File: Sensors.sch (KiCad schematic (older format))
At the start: 69 parts, among them CON1 CONSOLE, IC1 ATMEGA328P, P1 CONN_01X08, P10 GPIO, P11 I2C, P12 96B-GPIO, P13 96B-I2C0, P14 GPIO, P15 GPIO, P16 GPIO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

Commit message: Switch transistor schematic symbol to BC817
The part is still an S8050, but we want to use the SOT-23 footprint
instead of TO-92. The default Kicad libraries don't have a SOT-23
version of the S8050, but it does have one for the BC817 which uses the
same pinout. Switch the schematic symbol so that KiCad stops complaining
about the footprint being different and needing to be "rescued"

Signed-off-by: Grant Likely <grant.likely@linaro.org>
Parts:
- Q1: symbol S8050 -> BC817-40
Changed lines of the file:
@@
 NoConn ~ 5550 6800
 $Comp
-L S8050 Q1
+L BC817-40 Q1
 U 1 1 55CE16C0
 P 5150 1600

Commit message: Get rid of "Sensors2" library
All of the footprints are stored in the "Sensors" library. The extra
"Sendors2" library is no longer needed. Replace all references to it
with "Sensors".

Signed-off-by: Grant Likely <grant.likely@linaro.org>
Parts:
- Q1, U5: footprint Sensors2:SOT-23_Seeed -> Sensors:SOT-23_Seeed
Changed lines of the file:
@@
 F 0 "U5" H 8150 2450 60  0000 C CNN
 F 1 "XC6206" H 8350 2450 60  0000 L CNN
-F 2 "Sensors2:SOT-23_Seeed" H 8150 2150 60  0001 C CNN
+F 2 "Sensors:SOT-23_Seeed" H 8150 2150 60  0001 C CNN
 F 3 "" H 8150 2150 60  0000 C CNN
 F 4 "310030016" H 2450 850 60  0001 C CNN "Seeed SKU"
@@
 F 0 "Q1" H 4900 1850 50  0000 L CNN
 F 1 "S8050" H 4900 1750 50  0000 L CNN
-F 2 "Sensors2:SOT-23_Seeed" H 5350 1525 50  0001 L CIN
+F 2 "Sensors:SOT-23_Seeed" H 5350 1525 50  0001 L CIN
 F 3 "" H 5150 1600 50  0000 L CNN
 	1    5150 1600

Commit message: Change resistor footprint for Seeed manufacturing
The default resistor footprint doesn't work for Seeed. Replace with the
footprint used on the UART board.

Signed-off-by: Grant Likely <grant.likely@linaro.org>
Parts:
- R1, R10, R11, R12, R13, R14, R15, R16, R2, R3, R4, R5, R6, R7, R8, R9: footprint Resistors_SMD:R_0603 -> Sensors:R_0603_Seeed
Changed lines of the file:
@@
 F 0 "R4" V 5330 750 50  0000 C CNN
 F 1 "10K" V 5250 750 50  0000 C CNN
-F 2 "Resistors_SMD:R_0603" V 5180 750 30  0001 C CNN
+F 2 "Sensors:R_0603_Seeed" V 5180 750 30  0001 C CNN
 F 3 "" H 5250 750 30  0000 C CNN
 F 4 "301010299" H 5250 750 60  0001 C CNN "Seeed SKU"
@@
 F 0 "R6" V 6330 750 50  0000 C CNN
 F 1 "620R" V 6250 750 50  0000 C CNN
-F 2 "Resistors_SMD:R_0603" V 6180 750 30  0001 C CNN
+F 2 "Sensors:R_0603_Seeed" V 6180 750 30  0001 C CNN
 F 3 "" H 6250 750 30  0000 C CNN
 F 4 "301010210" H 6250 750 60  0001 C CNN "Seeed SKU"
@@
 F 0 "R5" V 5580 750 50  0000 C CNN
 F 1 "620R" V 5500 750 50  0000 C CNN
-F 2 "Resistors_SMD:R_0603" V 5430 750 30  0001 C CNN
+F 2 "Sensors:R_0603_Seeed" V 5430 750 30  0001 C CNN
 F 3 "" H 5500 750 30  0000 C CNN
 F 4 "301010210" H 5500 750 60  0001 C CNN "Seeed SKU"
@@
 F 0 "R8" V 8080 6000 50  0000 C CNN
 F 1 "620R" V 8000 6000 50  0000 C CNN
-F 2 "Resistors_SMD:R_0603" V 7930 6000 30  0001 C CNN
+F 2 "Sensors:R_0603_Seeed" V 7930 6000 30  0001 C CNN
 F 3 "" H 8000 6000 30  0000 C CNN
 F 4 "301010210" H 2450 850 60  0001 C CNN "Seeed SKU"
@@
 F 0 "R9" V 8230 6000 50  0000 C CNN
 F 1 "620R" V 8150 6000 50  0000 C CNN
-F 2 "Resistors_SMD:R_0603" V 8080 6000 30  0001 C CNN
+F 2 "Sensors:R_0603_Seeed" V 8080 6000 30  0001 C CNN
 F 3 "" H 8150 6000 30  0000 C CNN
 F 4 "301010210" H 2450 850 60  0001 C CNN "Seeed SKU"
@@
 F 0 "R10" V 8380 6000 50  0000 C CNN
 F 1 "620R" V 8300 6000 50  0000 C CNN
-F 2 "Resistors_SMD:R_0603" V 8230 6000 30  0001 C CNN
+F 2 "Sensors:R_0603_Seeed" V 8230 6000 30  0001 C CNN
 F 3 "" H 8300 6000 30  0000 C CNN
 F 4 "301010210" H 2450 850 60  0001 C CNN "Seeed SKU"
@@
 F 0 "R11" V 8530 6000 50  0000 C CNN
 F 1 "620R" V 8450 6000 50  0000 C CNN
-F 2 "Resistors_SMD:R_0603" V 8380 6000 30  0001 C CNN
+F 2 "Sensors:R_0603_Seeed" V 8380 6000 30  0001 C CNN
 F 3 "" H 8450 6000 30  0000 C CNN
 F 4 "301010210" H 2450 850 60  0001 C CNN "Seeed SKU"
@@
 F 0 "R7" V 6580 750 50  0000 C CNN
 F 1 "620R" V 6500 750 50  0000 C CNN
-F 2 "Resistors_SMD:R_0603" V 6430 750 30  0001 C CNN
+F 2 "Sensors:R_0603_Seeed" V 6430 750 30  0001 C CNN
 F 3 "" H 6500 750 30  0000 C CNN
 F 4 "301010210" H 6500 750 60  0001 C CNN "Seeed SKU"
@@
 F 0 "R1" V 2480 4100 50  0000 C CNN
 F 1 "22R" V 2400 4100 50  0000 C CNN
-F 2 "Resistors_SMD:R_0603" V 2330 4100 30  0001 C CNN
+F 2 "Sensors:R_0603_Seeed" V 2330 4100 30  0001 C CNN
 F 3 "" H 2400 4100 30  0000 C CNN
 F 4 "301010289" H 2400 4100 60  0001 C CNN "Seeed SKU"
@@
 F 0 "R2" V 2480 4200 50  0000 C CNN
 F 1 "22R" V 2400 4200 50  0000 C CNN
-F 2 "Resistors_SMD:R_0603" V 2330 4200 30  0001 C CNN
+F 2 "Sensors:R_0603_Seeed" V 2330 4200 30  0001 C CNN
 F 3 "" H 2400 4200 30  0000 C CNN
 F 4 "301010289" H 2450 850 60  0001 C CNN "Seeed SKU"
@@
 F 0 "R3" V 4180 4150 50  0000 C CNN
 F 1 "10K" V 4100 4150 50  0000 C CNN
-F 2 "Resistors_SMD:R_0603" V 4030 4150 30  0001 C CNN
+F 2 "Sensors:R_0603_Seeed" V 4030 4150 30  0001 C CNN
 F 3 "" H 4100 4150 30  0000 C CNN
 F 4 "301010299" H 2450 850 60  0001 C CNN "Seeed SKU"
@@
 F 0 "R12" V 5580 1750 50  0000 C CNN
 F 1 "620R" V 5500 1750 50  0000 C CNN
-F 2 "Resistors_SMD:R_0603" V 5430 1750 30  0001 C CNN
+F 2 "Sensors:R_0603_Seeed" V 5430 1750 30  0001 C CNN
 F 3 "" H 5500 1750 30  0000 C CNN
 F 4 "301010210" H 2450 850 60  0001 C CNN "Seeed SKU"
@@
 F 0 "R13" V 5030 1750 50  0000 C CNN
 F 1 "10K" V 4950 1750 50  0000 C CNN
-F 2 "Resistors_SMD:R_0603" V 4880 1750 30  0001 C CNN
+F 2 "Sensors:R_0603_Seeed" V 4880 1750 30  0001 C CNN
 F 3 "" H 4950 1750 30  0000 C CNN
 F 4 "301010299" H 2450 850 60  0001 C CNN "Seeed SKU"
@@
 F 0 "R14" V 4180 4550 50  0000 C CNN
 F 1 "220R" V 4100 4550 50  0000 C CNN
-F 2 "Resistors_SMD:R_0603" V 4030 4550 30  0001 C CNN
+F 2 "Sensors:R_0603_Seeed" V 4030 4550 30  0001 C CNN
 F 3 "" H 4100 4550 30  0000 C CNN
 F 4 "301010163" H 2450 850 60  0001 C CNN "Seeed SKU"
@@
 F 0 "R15" V 4180 4650 50  0000 C CNN
 F 1 "220R" V 4100 4650 50  0000 C CNN
-F 2 "Resistors_SMD:R_0603" V 4030 4650 30  0001 C CNN
+F 2 "Sensors:R_0603_Seeed" V 4030 4650 30  0001 C CNN
 F 3 "" H 4100 4650 30  0000 C CNN
 F 4 "301010163" H 2450 850 60  0001 C CNN "Seeed SKU"
@@
 F 0 "R16" V 4830 1600 50  0000 C CNN
 F 1 "620R" V 4750 1600 50  0000 C CNN
-F 2 "Resistors_SMD:R_0603" V 4680 1600 30  0001 C CNN
+F 2 "Sensors:R_0603_Seeed" V 4680 1600 30  0001 C CNN
 F 3 "" H 4750 1600 30  0000 C CNN
 	1    4750 1600

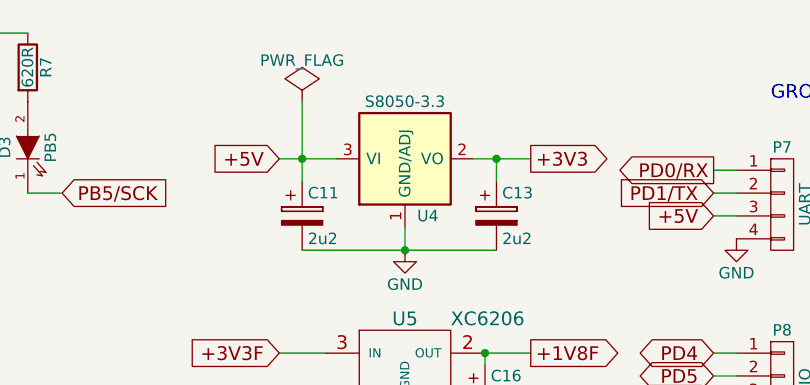
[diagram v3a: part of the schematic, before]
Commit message: Fix incorrect part specifier for 3.3V regulator
The V3.3 regulator is a CJT1117, not an S8050

Signed-off-by: Grant Likely <grant.likely@linaro.org>
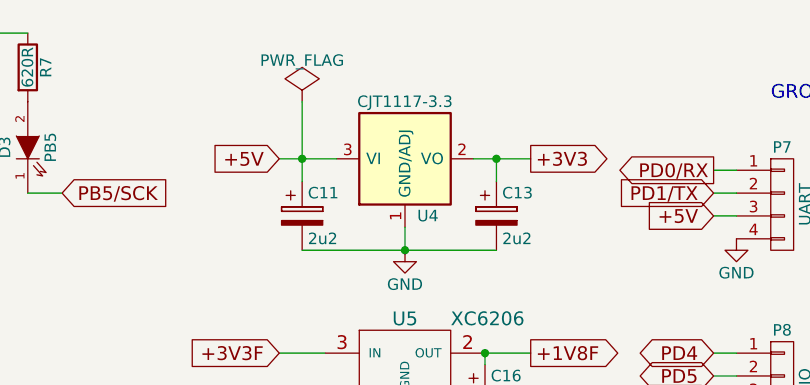
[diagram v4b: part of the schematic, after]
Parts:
- U4: value S8050-3.3 -> CJT1117-3.3
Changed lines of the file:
@@
 P 8150 1150
 F 0 "U4" H 8250 900 50  0000 C CNN
-F 1 "S8050-3.3" H 8150 1400 50  0000 C CNN
+F 1 "CJT1117-3.3" H 8150 1400 50  0000 C CNN
 F 2 "Sensors:SOT223" H 8150 1150 60  0001 C CNN
 F 3 "" H 8150 1150 60  0000 C CNN

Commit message: Update part numbers in schematic for BOM generation
Signed-off-by: Grant Likely <grant.likely@linaro.org>
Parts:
- Q1: Mfr Part # (none) -> S8050; Seeed SKU (none) -> 305010017
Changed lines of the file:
@@
 F 2 "Sensors:SOT-23_Seeed" H 5350 1525 50  0001 L CIN
 F 3 "" H 5150 1600 50  0000 L CNN
+F 4 "305010017" H 5150 1600 60  0001 C CNN "Seeed SKU"
+F 5 "S8050" H 5150 1600 60  0001 C CNN "Mfr Part #"
 	1    5150 1600
 	1    0    0    -1

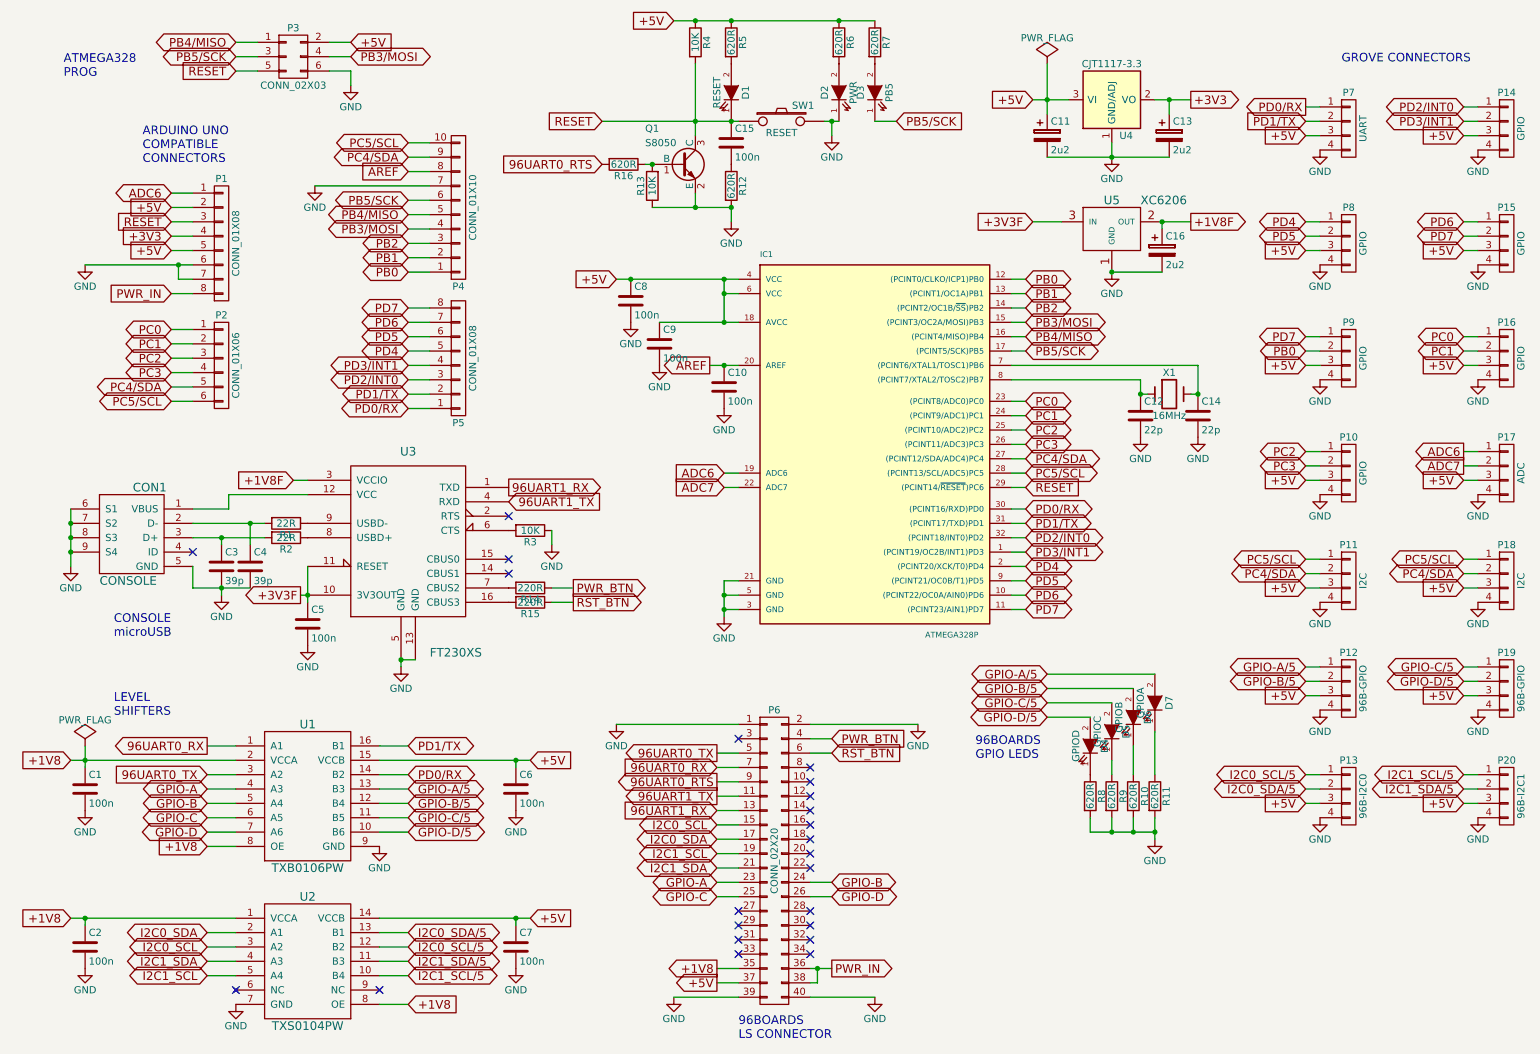
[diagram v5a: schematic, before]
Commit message: Remove the switch
Signed-off-by: Grant Likely <grant.likely@linaro.org>
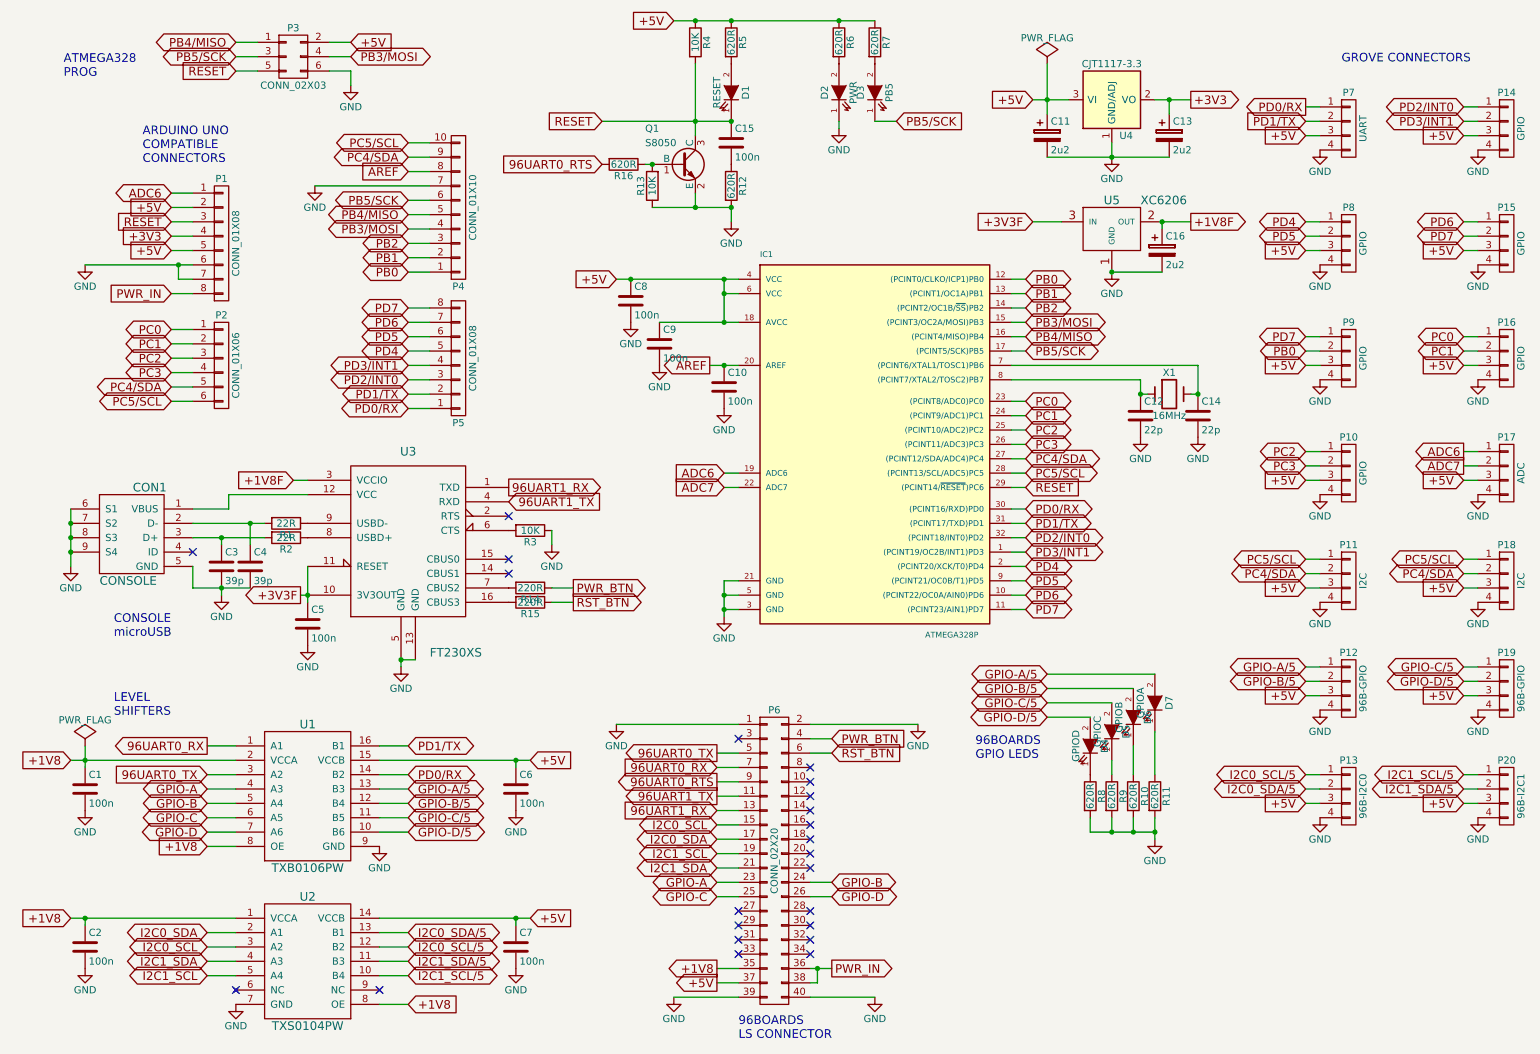
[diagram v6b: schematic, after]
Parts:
- removed SW1: RESET, Sensors:SW_PUSH_DTSM_62K, symbol SW_PUSH
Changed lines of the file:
@@
 LIBS:contrib
 LIBS:valves
-LIBS:GPlib
 LIBS:Sensors-cache
 EELAYER 25 0
@@
 	1    0    0    -1
 $EndComp
-$Comp
-L SW_PUSH SW1
-U 1 1 55BE860C
-P 5850 1300
-F 0 "SW1" H 6000 1410 50  0000 C CNN
-F 1 "RESET" H 5850 1220 50  0000 C CNN
-F 2 "Sensors:SW_PUSH_DTSM_62K" H 5850 1300 60  0001 C CNN
-F 3 "" H 5850 1300 60  0000 C CNN
-F 4 "311020004" H 2450 850 60  0001 C CNN "Seeed SKU"
-F 5 "DIPTRONICS" H 2450 850 60  0001 C CNN "Mfr"
-F 6 "DTSM-62K-S-V-T/R(SN431)" H 2450 850 60  0001 C CNN "Mfr Part #"
-	1    5850 1300
-	1    0    0    -1
-$EndComp
 Text GLabel 900  5750 0    60   Input ~ 0
 +1V8
@@
 L GND #PWR030
 U 1 1 55BFA7BD
-P 6200 1400
-F 0 "#PWR030" H 6200 1150 50  0001 C CNN
-F 1 "GND" H 6200 1250 50  0000 C CNN
-F 2 "" H 6200 1400 60  0000 C CNN
-F 3 "" H 6200 1400 60  0000 C CNN
-	1    6200 1400
+P 6250 1350
+F 0 "#PWR030" H 6250 1100 50  0001 C CNN
+F 1 "GND" H 6250 1200 50  0000 C CNN
+F 2 "" H 6250 1350 60  0000 C CNN
+F 3 "" H 6250 1350 60  0000 C CNN
+	1    6250 1350
 	1    0    0    -1
 $EndComp
@@
 	1750 3250 1600 3250
 Wire Wire Line
-	1000 2300 1750 2300
+	1000 2300 1650 2300
+Wire Wire Line
+	1650 2300 1750 2300
 Wire Wire Line
 	1750 2400 1650 2400
@@
 	7450 2900 7550 2900
 Wire Wire Line
-	4700 2400 5550 2400
+	4700 2400 4800 2400
+Wire Wire Line
+	4800 2400 5450 2400
+Wire Wire Line
+	5450 2400 5550 2400
 Wire Wire Line
 	5550 2500 5450 2500
 Wire Wire Line
-	5450 2400 5450 2700
+	5450 2400 5450 2500
+Wire Wire Line
+	5450 2500 5450 2700
 Connection ~ 5450 2400
 Connection ~ 4800 2400
 Wire Wire Line
-	5000 2700 5550 2700
-Wire Wire Line
-	5350 3000 5550 3000
+	5000 2700 5450 2700
+Wire Wire Line
+	5450 2700 5550 2700
+Wire Wire Line
+	5350 3000 5450 3000
+Wire Wire Line
+	5450 3000 5550 3000
 Wire Wire Line
 	7450 3000 8750 3000
@@
 	5550 4500 5450 4500
 Wire Wire Line
-	5450 4500 5450 4750
+	5450 4500 5450 4600
+Wire Wire Line
+	5450 4600 5450 4700
+Wire Wire Line
+	5450 4700 5450 4750
 Wire Wire Line
 	5450 4700 5550 4700
@@
 	5400 5800 5550 5800
 Wire Wire Line
-	8450 1150 8700 1150
-Wire Wire Line
-	7700 1550 8550 1550
+	8450 1150 8550 1150
+Wire Wire Line
+	8550 1150 8700 1150
+Wire Wire Line
+	7700 1550 8150 1550
+Wire Wire Line
+	8150 1550 8550 1550
 Wire Wire Line
 	8550 1250 8550 1150
@@
 Connection ~ 5500 600
 Wire Wire Line
-	4600 1300 5550 1300
+	4600 1300 5250 1300
+Wire Wire Line
+	5250 1300 5500 1300
 Connection ~ 5250 1300
 Connection ~ 5500 1300
 Wire Wire Line
-	5100 600  6500 600
-Wire Wire Line
-	6150 1300 6250 1300
-Wire Wire Line
-	6200 1400 6200 1300
-Connection ~ 6200 1300
+	5100 600  5250 600
+Wire Wire Line
+	5250 600  5500 600
+Wire Wire Line
+	5500 600  6250 600
+Wire Wire Line
+	6250 600  6500 600
 Wire Wire Line
 	1850 5650 2050 5650
 Wire Wire Line
-	900  5750 2050 5750
+	900  5750 1000 5750
+Wire Wire Line
+	1000 5750 2050 5750
 Connection ~ 1000 5750
 Wire Wire Line
-	1000 5650 1000 5800
+	1000 5650 1000 5750
+Wire Wire Line
+	1000 5750 1000 5800
 Wire Wire Line
 	3050 5650 3250 5650
 Wire Wire Line
-	3050 5750 4100 5750
+	3050 5750 4000 5750
+Wire Wire Line
+	4000 5750 4100 5750
 Connection ~ 4000 5750
 Wire Wire Line
@@
 	3250 7450 3050 7450
 Wire Wire Line
-	900  6850 2050 6850
+	900  6850 1000 6850
+Wire Wire Line
+	1000 6850 2050 6850
 Wire Wire Line
 	1000 6900 1000 6850
@@
 	5550 5500 4700 5500
 Wire Wire Line
-	3050 6850 4100 6850
+	3050 6850 4000 6850
+Wire Wire Line
+	4000 6850 4100 6850
 Wire Wire Line
 	4000 6900 4000 6850
@@
 	8150 5750 8150 5850
 Wire Wire Line
-	8000 6250 8450 6250
-Wire Wire Line
-	8450 6150 8450 6300
+	8000 6250 8150 6250
+Wire Wire Line
+	8150 6250 8300 6250
+Wire Wire Line
+	8300 6250 8450 6250
+Wire Wire Line
+	8450 6150 8450 6250
+Wire Wire Line
+	8450 6250 8450 6300
 Wire Wire Line
 	8000 6150 8000 6250
@@
 Connection ~ 8150 1550
 Wire Wire Line
-	7700 900  7700 1250
+	7700 900  7700 1150
+Wire Wire Line
+	7700 1150 7700 1250
 Connection ~ 7700 1150
 Connection ~ 6250 600
@@
 	5400 6100 5550 6100
 Wire Wire Line
-	900  4000 900  4400
+	900  4000 900  4100
+Wire Wire Line
+	900  4100 900  4200
+Wire Wire Line
+	900  4200 900  4300
+Wire Wire Line
+	900  4300 900  4400
 Connection ~ 900  4100
 Connection ~ 900  4200
 Connection ~ 900  4300
 Wire Wire Line
-	1750 4100 2250 4100
-Wire Wire Line
-	1750 4200 2250 4200
+	1750 4100 2150 4100
+Wire Wire Line
+	2150 4100 2250 4100
+Wire Wire Line
+	1750 4200 1950 4200
+Wire Wire Line
+	1950 4200 2250 4200
 Wire Wire Line
 	2150 4250 2150 4100
@@
 	1750 4400 1750 4550
 Wire Wire Line
-	1750 4550 2150 4550
+	1750 4550 1950 4550
+Wire Wire Line
+	1950 4550 2150 4550
 Connection ~ 1950 4550
 Wire Wire Line
@@
 	2000 3900 2550 3900
 Wire Wire Line
-	2550 4400 2550 4650
+	2550 4400 2550 4600
+Wire Wire Line
+	2550 4600 2550 4650
 Connection ~ 2550 4600
 Wire Wire Line
@@
 	6100 7300 6100 7200
 Wire Wire Line
-	6050 7200 6200 7200
+	6050 7200 6100 7200
+Wire Wire Line
+	6100 7200 6200 7200
 Connection ~ 6100 7200
 NoConn ~ 1750 4300
@@
 	8500 2050 8500 2000
 Wire Wire Line
-	7600 1150 7850 1150
+	7600 1150 7700 1150
+Wire Wire Line
+	7700 1150 7850 1150
 Text GLabel 2500 4600 0    60   Output ~ 0
 +3V3F
@@
 $EndComp
 Wire Wire Line
-	4950 1900 5500 1900
+	4950 1900 5250 1900
+Wire Wire Line
+	5250 1900 5500 1900
 Connection ~ 5500 1900
 Wire Wire Line
-	5250 900  5250 1400
+	5250 900  5250 1300
+Wire Wire Line
+	5250 1300 5250 1400
 $Comp
 L R R16
@@
 	5250 1800 5250 1900
 Connection ~ 5250 1900
+Wire Wire Line
+	6250 1350 6250 1300
 $EndSCHEMATC
